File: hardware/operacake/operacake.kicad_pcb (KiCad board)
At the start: 4 copper layers, 120 x 75 mm, 152 parts, among them J1 CONN_02X20, J2 CONN_02X20, P1 ADDRESS, P20 GPIO, P22 I2S, P28 SD, P9 BASEBAND, U1 MASWSS0129, U10 74LVC1G58, U11 74LVC1G58, U12 74LVC1G58, U13 74LVC1G58, U14 74AHC1G02, U15 74AHC1G02, U16 74LVC1G19, U2 SKY13322, U3 SKY13322, U4 PCA9557, U5 TC7MBL3245CFT, U6 74LVC1G58, U7 74LVC1G58, U8 74AHC1G08, U9 74AHC1G08

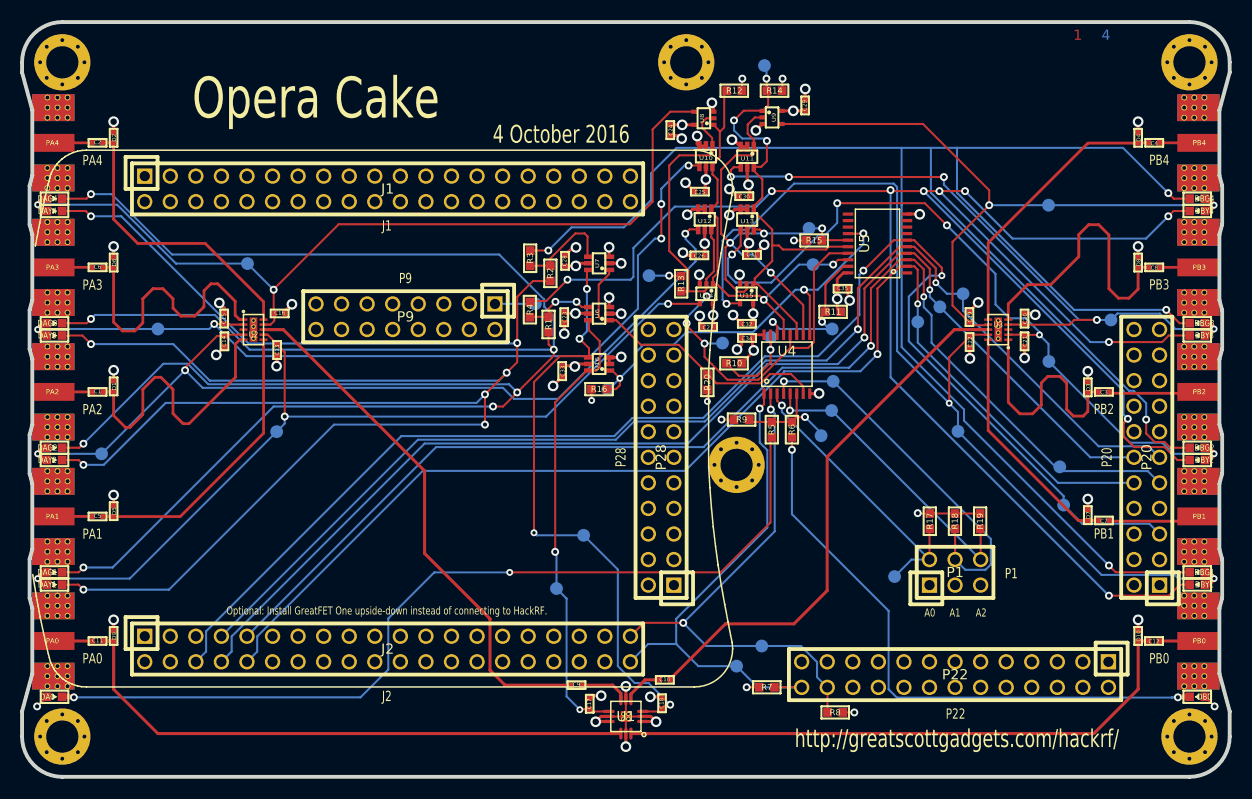
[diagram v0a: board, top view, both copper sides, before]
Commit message: Changed schematic and PCB to a design that seperates the PA & PB sides. No crossover will be possible with this design.
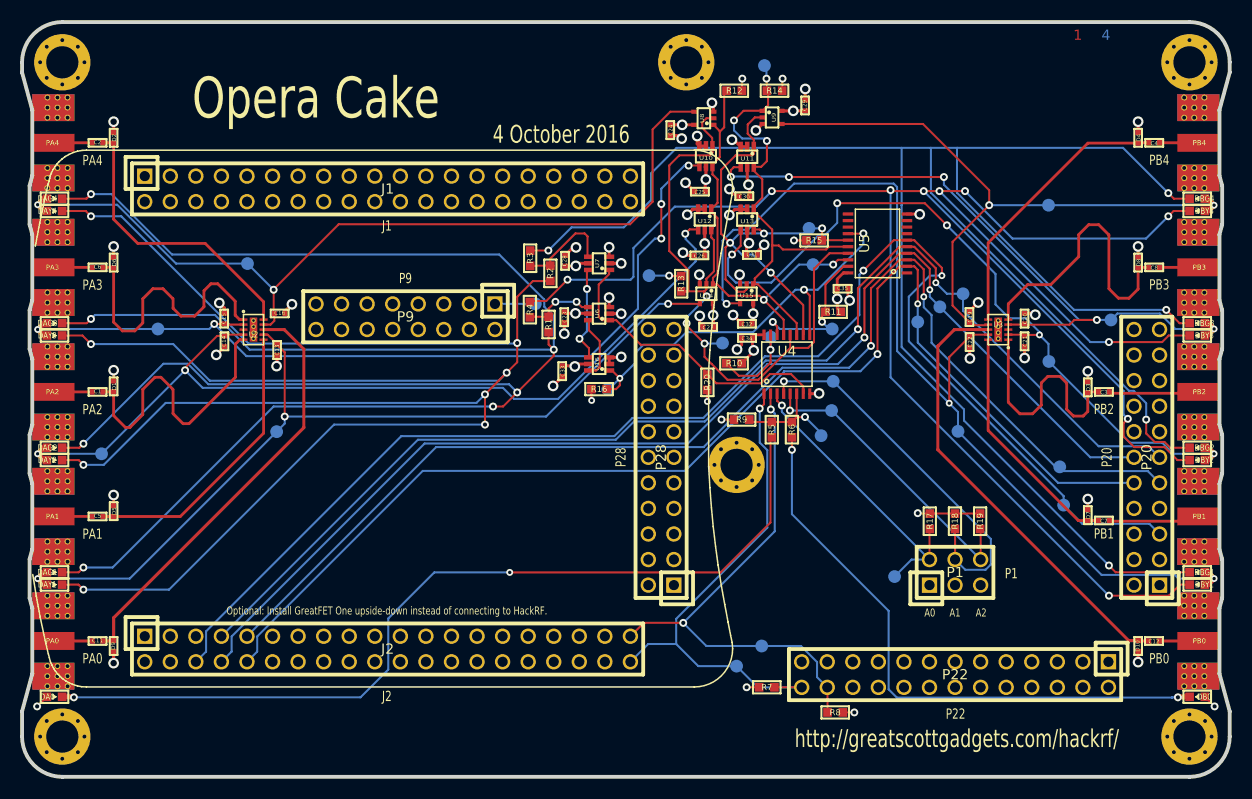
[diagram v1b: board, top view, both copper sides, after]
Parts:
- removed C10, C9: 100nF, gsg-modules:0402
- removed C17, C18: 33pF, gsg-modules:0402
- removed TP16, TP17: CONN_1, gsg-modules:TESTPOINT-50MIL
- removed U1: MASWSS0129, gsg-modules:QFN12-3
- moved D10 1.00 mm to (170.9, 162.0), turned to 270 degrees
- moved D9 1.00 mm to (69.1, 162.0), turned to 270 degrees
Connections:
- U16 pad 6: /U1VC2 -> Net-(U16-Pad6)
- U2 pad 8: Net-(C9-Pad2) -> Net-(C11-Pad1)
- U3 pad 8: Net-(C10-Pad1) -> Net-(C12-Pad1)
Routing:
- net Net-(C10-Pad1): track 53.8 -> 0.00 mm
- net Net-(C9-Pad2): track 53.0 -> 0.00 mm
- net /U1VC1: track 60.1 -> 9.36 mm, vias 4 -> 2
- net /U1VC2: track 45.8 -> 5.59 mm, vias 2 -> 0
- net GND: track 92.6 -> 73.8 mm, vias 52 -> 46
- net Net-(C11-Pad1): track 58.1 -> 42.7 mm
- net Net-(C12-Pad1): track 58.0 -> 44.8 mm
- net Net-(C9-Pad1): track 5.14 -> 0.00 mm
- net Net-(C10-Pad2): track 3.95 -> 0.00 mm
- net Net-(U16-Pad6): track 0.00 -> 1.17 mm

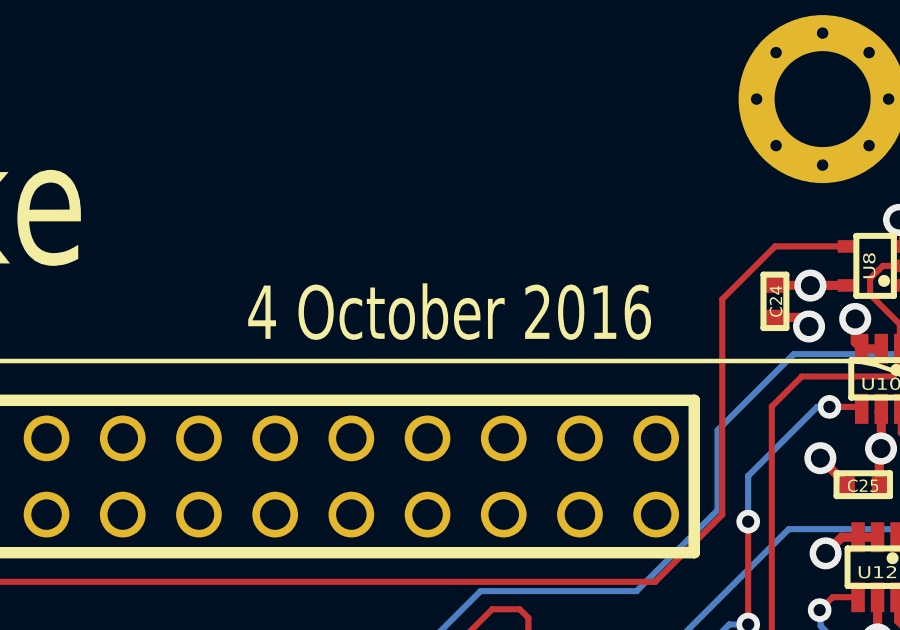
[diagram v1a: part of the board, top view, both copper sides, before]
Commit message: Changed date on silkscreen.
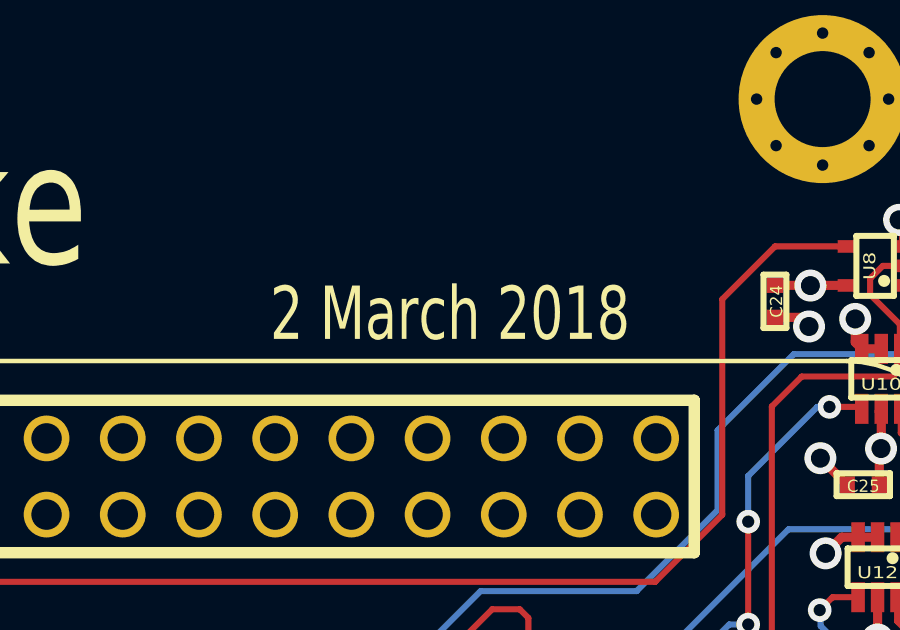
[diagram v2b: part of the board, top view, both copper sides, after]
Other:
- board text added: "2 March 2018"
- board text removed: "4 October 2016"
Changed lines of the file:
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@@
     (links 570)
     (no_connects 1)
-    (area 59.809499 99.809499 180.190501 175.190501)
+    (area 57.771558 99.809499 182.228443 175.190501)
     (thickness 1.6002)
     (drawings 148)
@@
   )
   (setup
-    (last_trace_width 0.3048)
+    (last_trace_width 0.2794)
     (user_trace_width 0.1524)
     (user_trace_width 0.2032)
@@
     (visible_elements FFFEFF7F)
     (pcbplotparams
-      (layerselection 0x00008_00000000)
+      (layerselection 0x012ff_80000007)
       (usegerberextensions true)
       (excludeedgelayer true)
@@
       (psnegative false)
       (psa4output false)
-      (plotreference false)
+      (plotreference true)
       (plotvalue false)
       (plotinvisibletext false)
@@
     (effects (font (size 1.016 1.016) (thickness 0.1778)))
   )
-  (gr_text "4 October 2016" (at 113.58 111.17) (layer F.SilkS)
+  (gr_text "2 March 2018" (at 113.58 111.17) (layer F.SilkS)
     (effects (font (size 1.778 1.27) (thickness 0.3048)))
   )
